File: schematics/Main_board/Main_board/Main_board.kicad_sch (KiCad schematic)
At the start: 10 parts, among them Q1 UMH3N, U1 ESP32-S3-WROOM-1, U4 CH340G, Y1 Crystal_GND2_Small

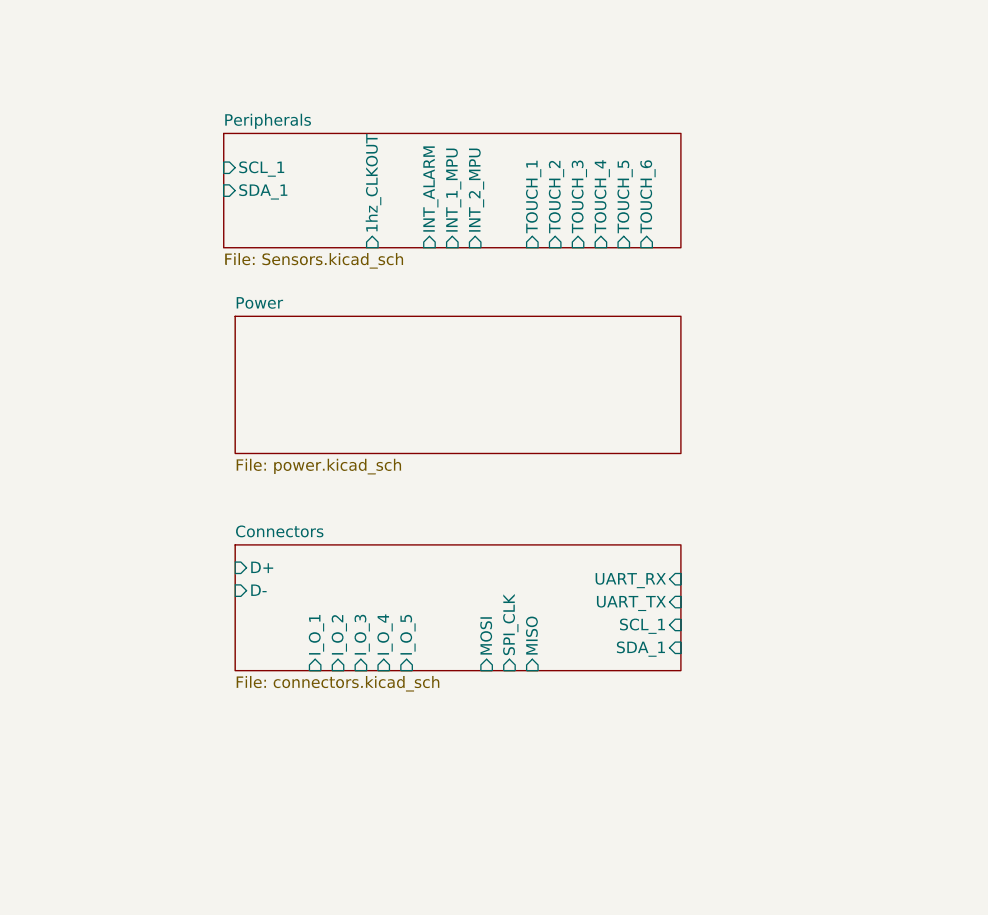
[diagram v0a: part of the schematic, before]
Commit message: update: All the resistors and capacitors footprints changed from 0603 to 0402
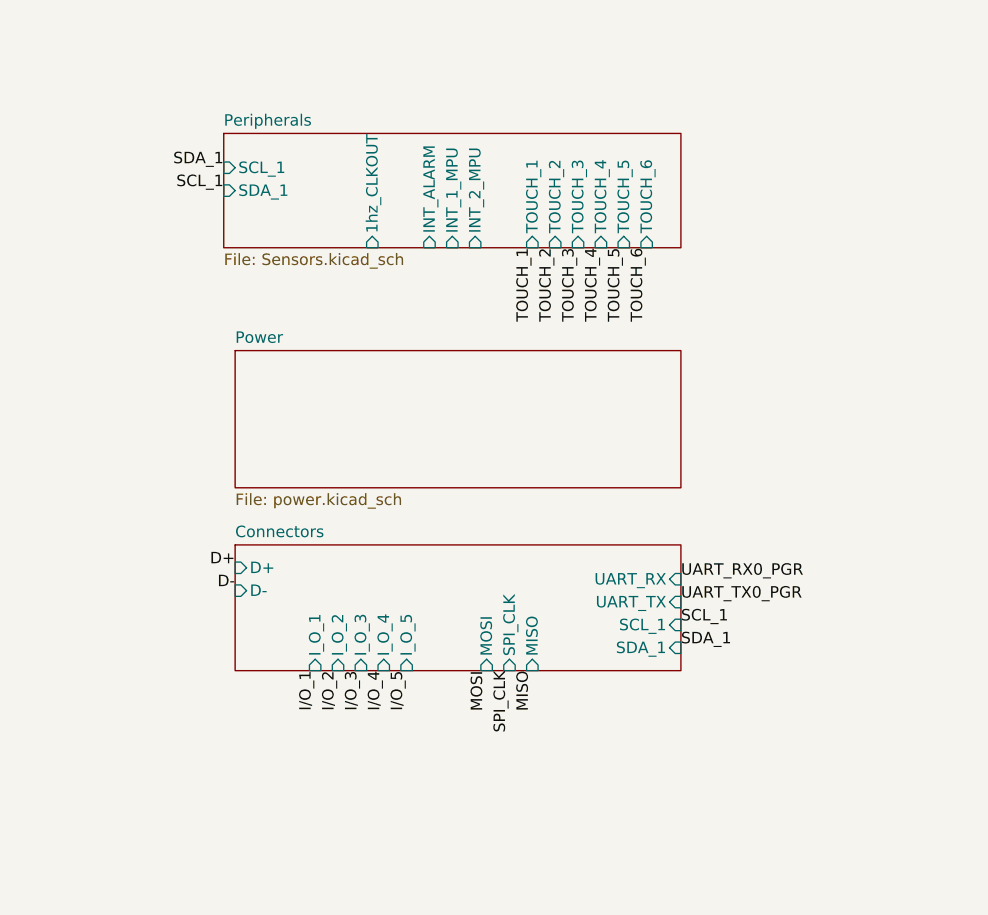
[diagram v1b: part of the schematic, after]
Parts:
- Y1: footprint Crystal:Resonator_SMD_Murata_CSTxExxV-3Pin_3.0x1.1mm_HandSoldering -> Crystal:Resonator_SMD_Murata_CSTxExxV-3Pin_3.0x1.1mm
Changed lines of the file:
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@@
     (effects (font (size 1.27 1.27)) (justify left bottom))
+  )
+  (label "TOUCH_2" (at 237.49 36.83 270) (fields_autoplaced)
+    (effects (font (size 1.27 1.27)) (justify right bottom))
   )
   (label "UART_RX0_PGR" (at 64.135 151.13 0) (fields_autoplaced)
@@
     (effects (font (size 1.27 1.27)) (justify right bottom))
   )
+  (label "I{slash}O_2" (at 213.36 83.82 270) (fields_autoplaced)
+    (effects (font (size 1.27 1.27)) (justify right bottom))
+  )
+  (label "SPI_CLK" (at 232.41 83.82 270) (fields_autoplaced)
+    (effects (font (size 1.27 1.27)) (justify right bottom))
+  )
   (label "TOUCH_4" (at 26.035 49.53 180) (fields_autoplaced)
     (effects (font (size 1.27 1.27)) (justify right bottom))
@@
     (effects (font (size 1.27 1.27)) (justify right bottom))
   )
+  (label "TOUCH_4" (at 242.57 36.83 270) (fields_autoplaced)
+    (effects (font (size 1.27 1.27)) (justify right bottom))
+  )
   (label "SPI_CLK" (at 26.035 57.15 180) (fields_autoplaced)
     (effects (font (size 1.27 1.27)) (justify right bottom))
@@
     (effects (font (size 1.27 1.27)) (justify left bottom))
   )
+  (label "SDA_1" (at 200.66 27.94 180) (fields_autoplaced)
+    (effects (font (size 1.27 1.27)) (justify right bottom))
+  )
   (label "DTR" (at 64.135 166.37 0) (fields_autoplaced)
     (effects (font (size 1.27 1.27)) (justify left bottom))
   )
+  (label "I{slash}O_4" (at 218.44 83.82 270) (fields_autoplaced)
+    (effects (font (size 1.27 1.27)) (justify right bottom))
+  )
   (label "UART_RX0_PGR" (at 146.304 31.75 0) (fields_autoplaced)
     (effects (font (size 1.27 1.27)) (justify left bottom))
@@
     (effects (font (size 1.27 1.27)) (justify right bottom))
   )
+  (label "TOUCH_6" (at 247.65 36.83 270) (fields_autoplaced)
+    (effects (font (size 1.27 1.27)) (justify right bottom))
+  )
+  (label "MOSI" (at 229.87 83.82 270) (fields_autoplaced)
+    (effects (font (size 1.27 1.27)) (justify right bottom))
+  )
+  (label "MISO" (at 234.95 83.82 270) (fields_autoplaced)
+    (effects (font (size 1.27 1.27)) (justify right bottom))
+  )
   (label "D+" (at 40.005 156.21 180) (fields_autoplaced)
     (effects (font (size 1.27 1.27)) (justify right bottom))
   )
+  (label "TOUCH_1" (at 234.95 36.83 270) (fields_autoplaced)
+    (effects (font (size 1.27 1.27)) (justify right bottom))
+  )
   (label "I{slash}O_1" (at 26.035 29.21 180) (fields_autoplaced)
     (effects (font (size 1.27 1.27)) (justify right bottom))
   )
+  (label "TOUCH_3" (at 240.03 36.83 270) (fields_autoplaced)
+    (effects (font (size 1.27 1.27)) (justify right bottom))
+  )
+  (label "SCL_1" (at 251.46 78.74 0) (fields_autoplaced)
+    (effects (font (size 1.27 1.27)) (justify left bottom))
+  )
   (label "TOUCH_5" (at 26.035 52.07 180) (fields_autoplaced)
     (effects (font (size 1.27 1.27)) (justify right bottom))
   )
+  (label "SDA_1" (at 251.46 81.28 0) (fields_autoplaced)
+    (effects (font (size 1.27 1.27)) (justify left bottom))
+  )
   (label "MISO" (at 26.035 59.69 180) (fields_autoplaced)
     (effects (font (size 1.27 1.27)) (justify right bottom))
@@
     (effects (font (size 1.27 1.27)) (justify right bottom))
   )
+  (label "I{slash}O_3" (at 215.9 83.82 270) (fields_autoplaced)
+    (effects (font (size 1.27 1.27)) (justify right bottom))
+  )
+  (label "D+" (at 201.93 72.39 180) (fields_autoplaced)
+    (effects (font (size 1.27 1.27)) (justify right bottom))
+  )
   (label "DTR" (at 92.71 160.02 180) (fields_autoplaced)
     (effects (font (size 1.27 1.27)) (justify right bottom))
@@
     (effects (font (size 1.27 1.27)) (justify right bottom))
   )
+  (label "SCL_1" (at 200.66 30.48 180) (fields_autoplaced)
+    (effects (font (size 1.27 1.27)) (justify right bottom))
+  )
+  (label "I{slash}O_1" (at 210.82 83.82 270) (fields_autoplaced)
+    (effects (font (size 1.27 1.27)) (justify right bottom))
+  )
+  (label "UART_RX0_PGR" (at 251.46 73.66 0) (fields_autoplaced)
+    (effects (font (size 1.27 1.27)) (justify left bottom))
+  )
+  (label "D-" (at 201.93 74.93 180) (fields_autoplaced)
+    (effects (font (size 1.27 1.27)) (justify right bottom))
+  )
+  (label "UART_TX0_PGR" (at 251.46 76.2 0) (fields_autoplaced)
+    (effects (font (size 1.27 1.27)) (justify left bottom))
+  )
+  (label "TOUCH_5" (at 245.11 36.83 270) (fields_autoplaced)
+    (effects (font (size 1.27 1.27)) (justify right bottom))
+  )
   (label "D-" (at 40.005 158.75 180) (fields_autoplaced)
+    (effects (font (size 1.27 1.27)) (justify right bottom))
+  )
+  (label "I{slash}O_5" (at 220.98 83.82 270) (fields_autoplaced)
     (effects (font (size 1.27 1.27)) (justify right bottom))
   )
@@
       (effects (font (size 1.27 1.27)))
     )
-    (property "Footprint" "Crystal:Resonator_SMD_Murata_CSTxExxV-3Pin_3.0x1.1mm_HandSoldering" (at 30.988 163.83 0)
+    (property "Footprint" "Crystal:Resonator_SMD_Murata_CSTxExxV-3Pin_3.0x1.1mm" (at 30.988 163.83 0)
       (effects (font (size 1.27 1.27)) hide)
     )
@@
     )
   )
-  (sheet (at 201.93 44.45) (size 49.53 15.24) (fields_autoplaced)
+  (sheet (at 201.93 48.26) (size 49.53 15.24) (fields_autoplaced)
     (stroke (width 0.1524) (type solid))
     (fill (color 0 0 0 0.0000))
-    (property "Sheetname" "Power" (at 201.93 43.7384 0)
+    (property "Sheetname" "Power" (at 201.93 47.5484 0)
       (effects (font (size 1.27 1.27)) (justify left bottom))
     )
-    (property "Sheetfile" "power.kicad_sch" (at 201.93 60.2746 0)
+    (property "Sheetfile" "power.kicad_sch" (at 201.93 64.0846 0)
       (effects (font (size 1.27 1.27)) (justify left top))
     )
@@
     )
     (property "Sheetfile" "connectors.kicad_sch" (at 201.93 84.4046 0)
-      (effects (font (size 1.27 1.27)) (justify left top))
+      (effects (font (size 1.27 1.27)) (justify left top) hide)
     )
     (pin "I_O_2" input (at 213.36 83.82 270)
